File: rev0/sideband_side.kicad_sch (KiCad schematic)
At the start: 28 parts, among them IC1 ECP5-BGA256, U8 USB3343-CP

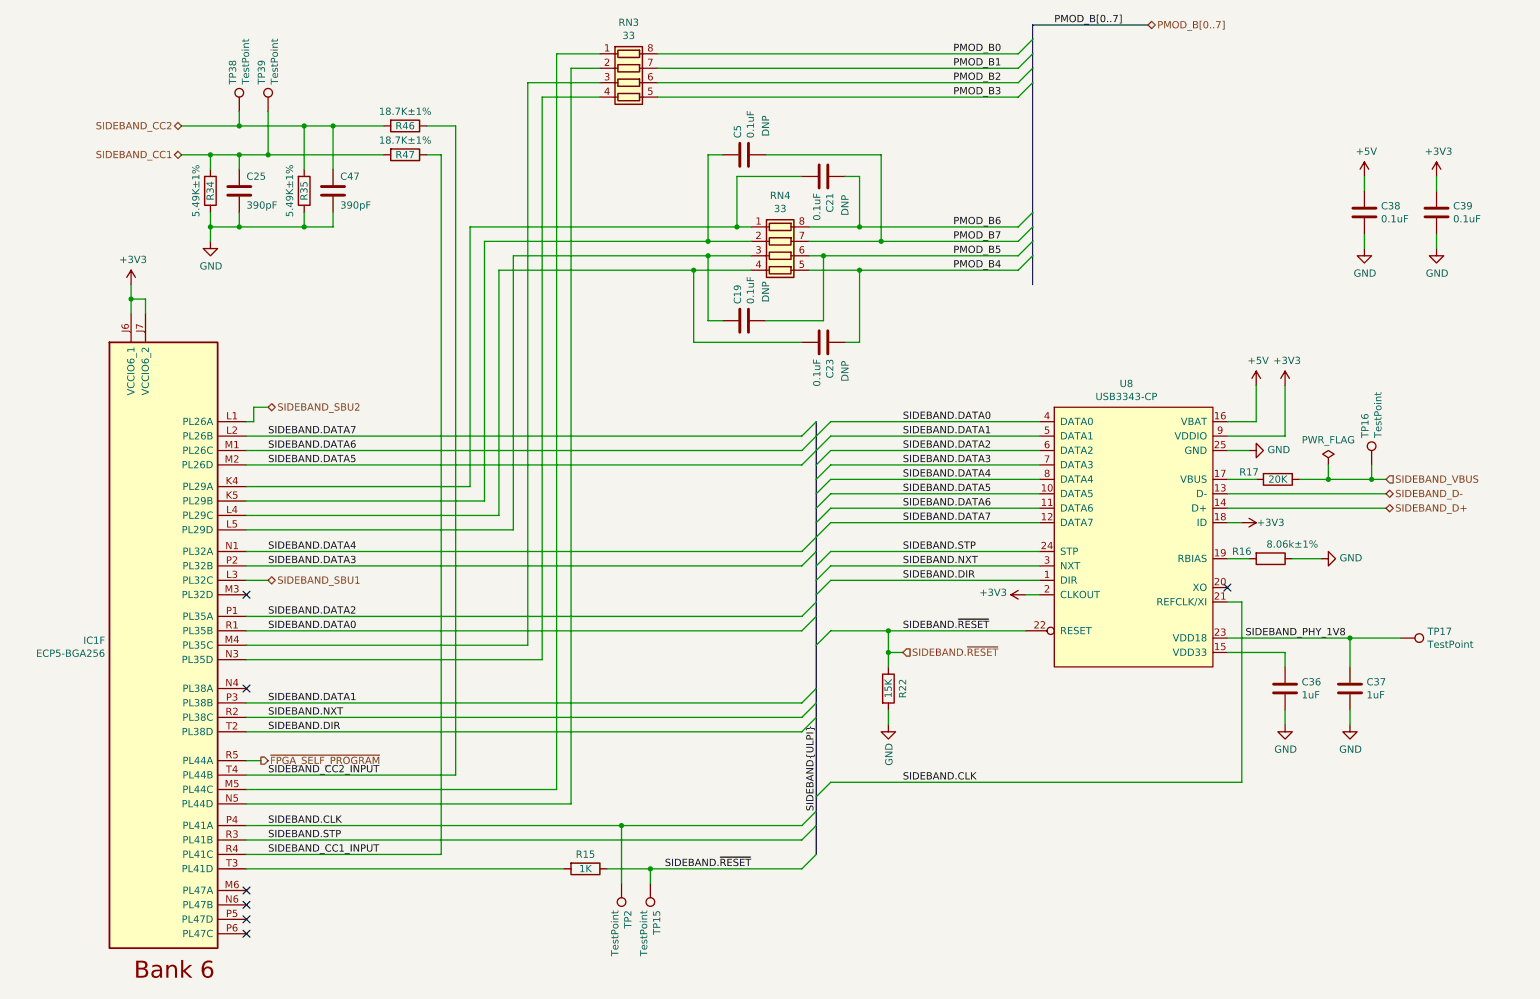
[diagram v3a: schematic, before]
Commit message: hardware: consistently use lowercase k for kilo
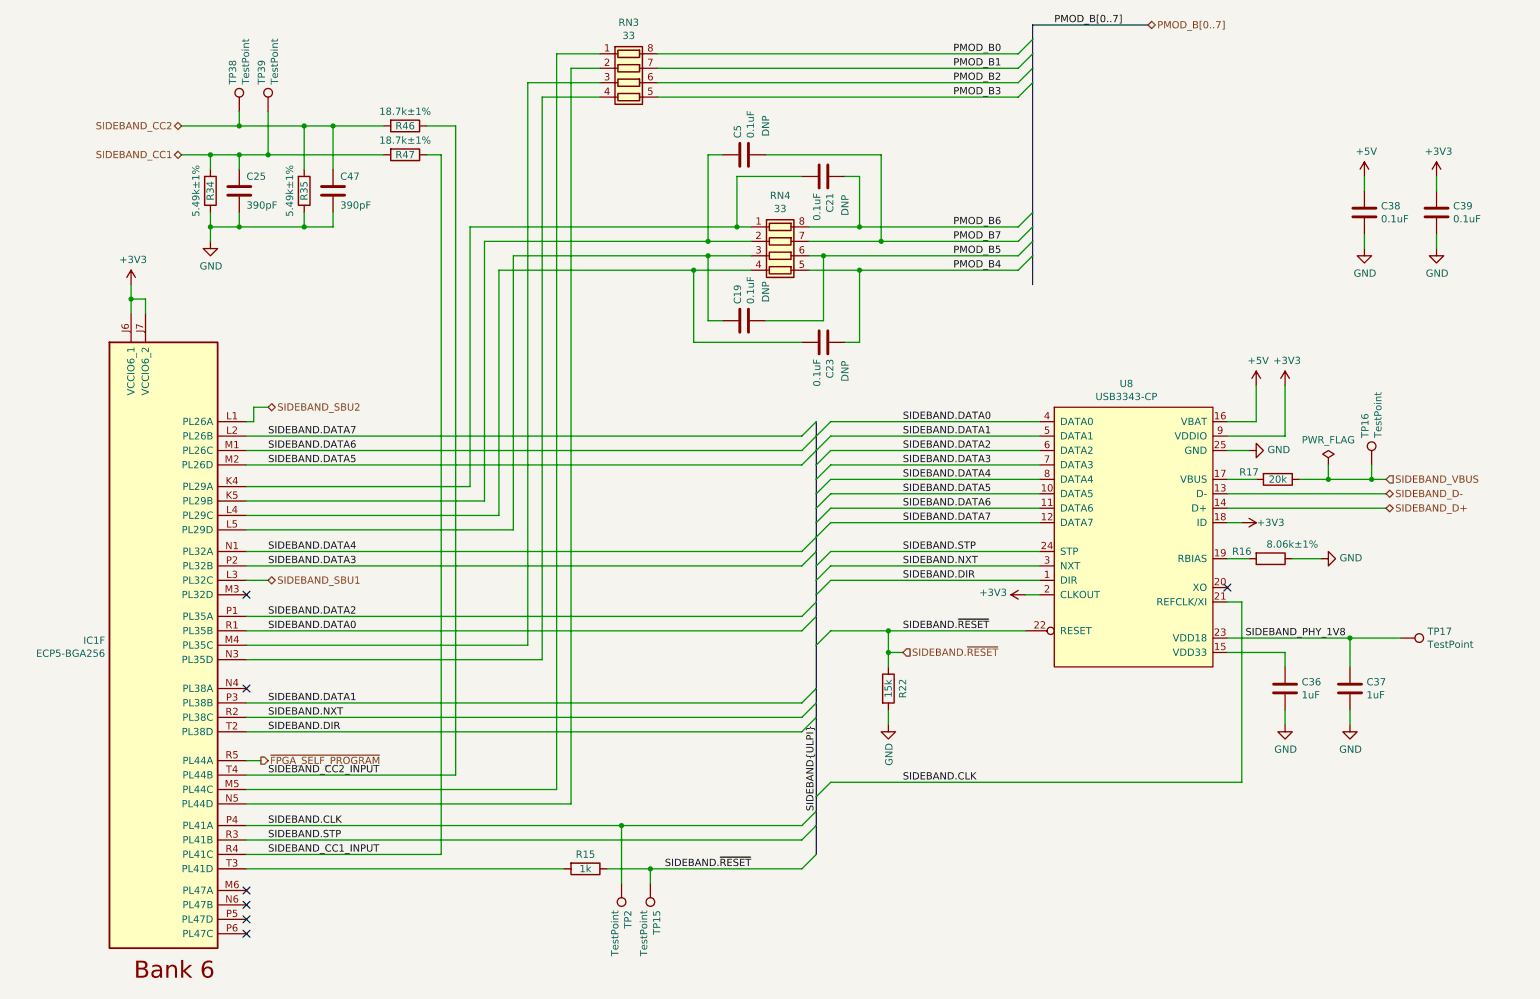
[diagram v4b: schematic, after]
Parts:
- R15: value 1K -> 1k
- R17: value 20K -> 20k
- R22: value 15K -> 15k
- R34, R35: value 5.49K±1% -> 5.49k±1%
- R46, R47: value 18.7K±1% -> 18.7k±1%
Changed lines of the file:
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@@
     (in_bom yes) (on_board yes)
     (property "Reference" "R17" (id 0) (at 229.87 95.25 90))
-    (property "Value" "20K" (id 1) (at 234.95 96.52 90))
+    (property "Value" "20k" (id 1) (at 234.95 96.52 90))
     (property "Footprint" "Resistor_SMD:R_0402_1005Metric" (id 2) (at 234.95 94.742 90)
       (effects (font (size 1.27 1.27)) hide)
@@
     (in_bom yes) (on_board yes)
     (property "Reference" "R15" (id 0) (at 113.03 162.56 90))
-    (property "Value" "1K" (id 1) (at 113.03 165.1 90))
+    (property "Value" "1k" (id 1) (at 113.03 165.1 90))
     (property "Footprint" "Resistor_SMD:R_0402_1005Metric" (id 2) (at 113.03 163.322 90)
       (effects (font (size 1.27 1.27)) hide)
@@
     (in_bom yes) (on_board yes)
     (property "Reference" "R22" (id 0) (at 168.91 133.35 90))
-    (property "Value" "15K" (id 1) (at 166.37 133.35 90))
+    (property "Value" "15k" (id 1) (at 166.37 133.35 90))
     (property "Footprint" "Resistor_SMD:R_0402_1005Metric" (id 2) (at 164.592 133.35 90)
       (effects (font (size 1.27 1.27)) hide)
@@
     (in_bom yes) (on_board yes)
     (property "Reference" "R46" (id 0) (at 81.28 34.29 90))
-    (property "Value" "18.7K±1%" (id 1) (at 81.28 31.75 90))
+    (property "Value" "18.7k±1%" (id 1) (at 81.28 31.75 90))
     (property "Footprint" "Resistor_SMD:R_0402_1005Metric" (id 2) (at 81.28 32.512 90)
       (effects (font (size 1.27 1.27)) hide)
@@
     (in_bom yes) (on_board yes)
     (property "Reference" "R47" (id 0) (at 81.28 39.37 90))
-    (property "Value" "18.7K±1%" (id 1) (at 81.28 36.83 90))
+    (property "Value" "18.7k±1%" (id 1) (at 81.28 36.83 90))
     (property "Footprint" "Resistor_SMD:R_0402_1005Metric" (id 2) (at 81.28 37.592 90)
       (effects (font (size 1.27 1.27)) hide)
@@
     (in_bom yes) (on_board yes)
     (property "Reference" "R34" (id 0) (at 46.99 45.72 90))
-    (property "Value" "5.49K±1%" (id 1) (at 44.45 45.72 90))
+    (property "Value" "5.49k±1%" (id 1) (at 44.45 45.72 90))
     (property "Footprint" "Resistor_SMD:R_0402_1005Metric" (id 2) (at 45.212 45.72 90)
       (effects (font (size 1.27 1.27)) hide)
@@
     (in_bom yes) (on_board yes)
     (property "Reference" "R35" (id 0) (at 63.5 45.72 90))
-    (property "Value" "5.49K±1%" (id 1) (at 60.96 45.72 90))
+    (property "Value" "5.49k±1%" (id 1) (at 60.96 45.72 90))
     (property "Footprint" "Resistor_SMD:R_0402_1005Metric" (id 2) (at 61.722 45.72 90)
       (effects (font (size 1.27 1.27)) hide)

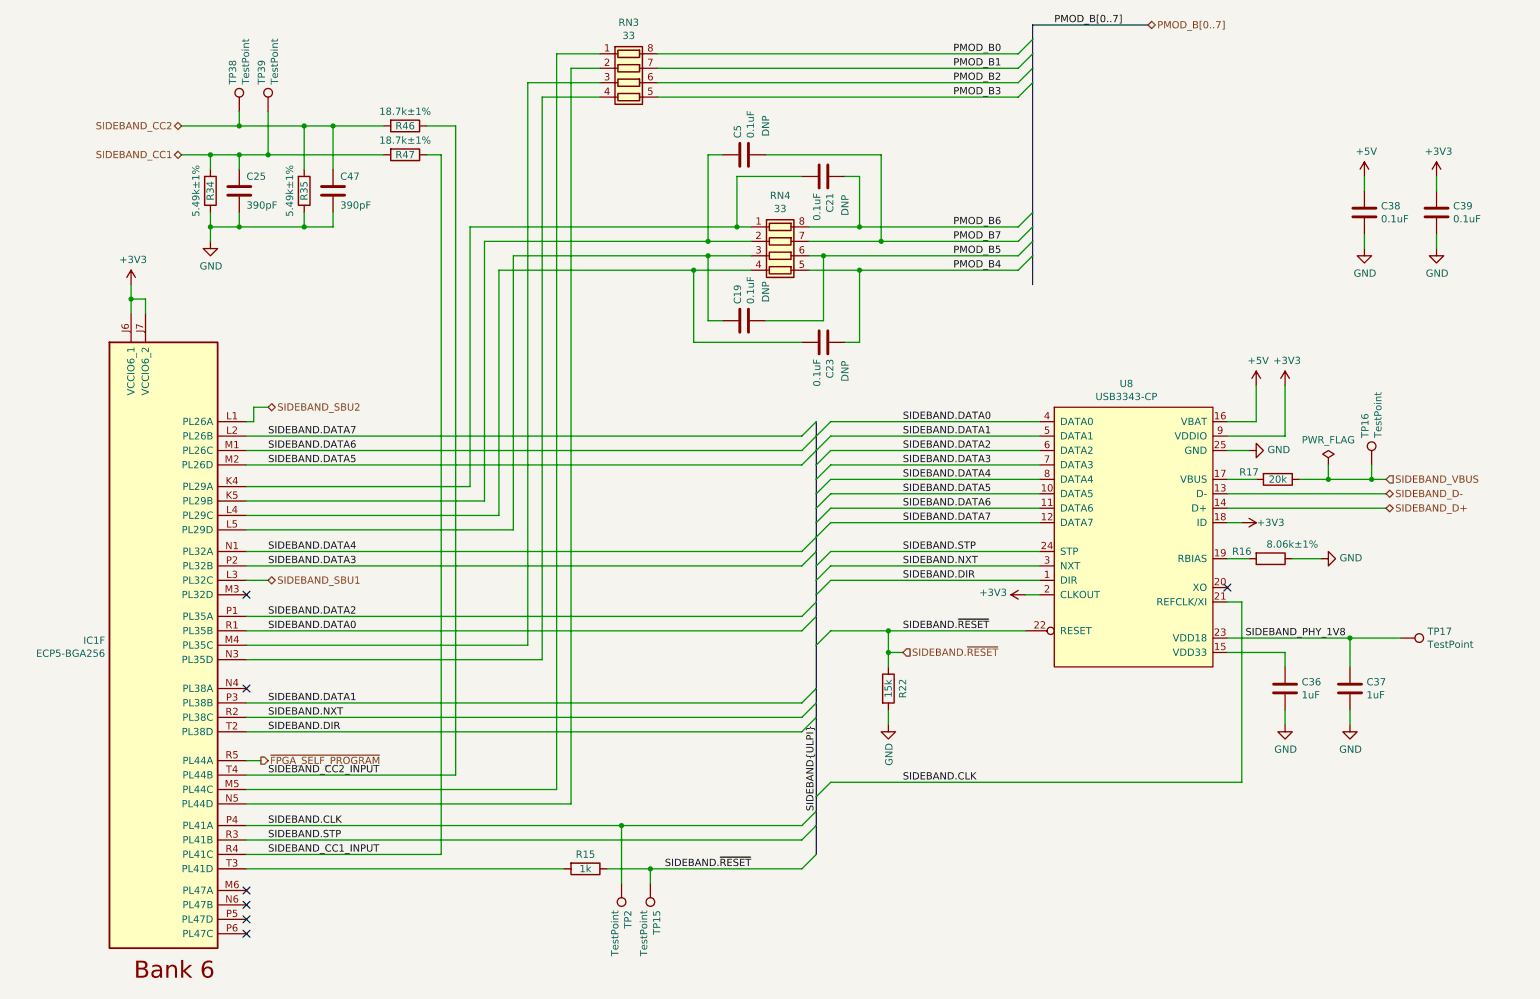
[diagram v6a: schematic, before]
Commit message: hardware: reassign FPGA I/O banks
assign HyperRAM to DQS group
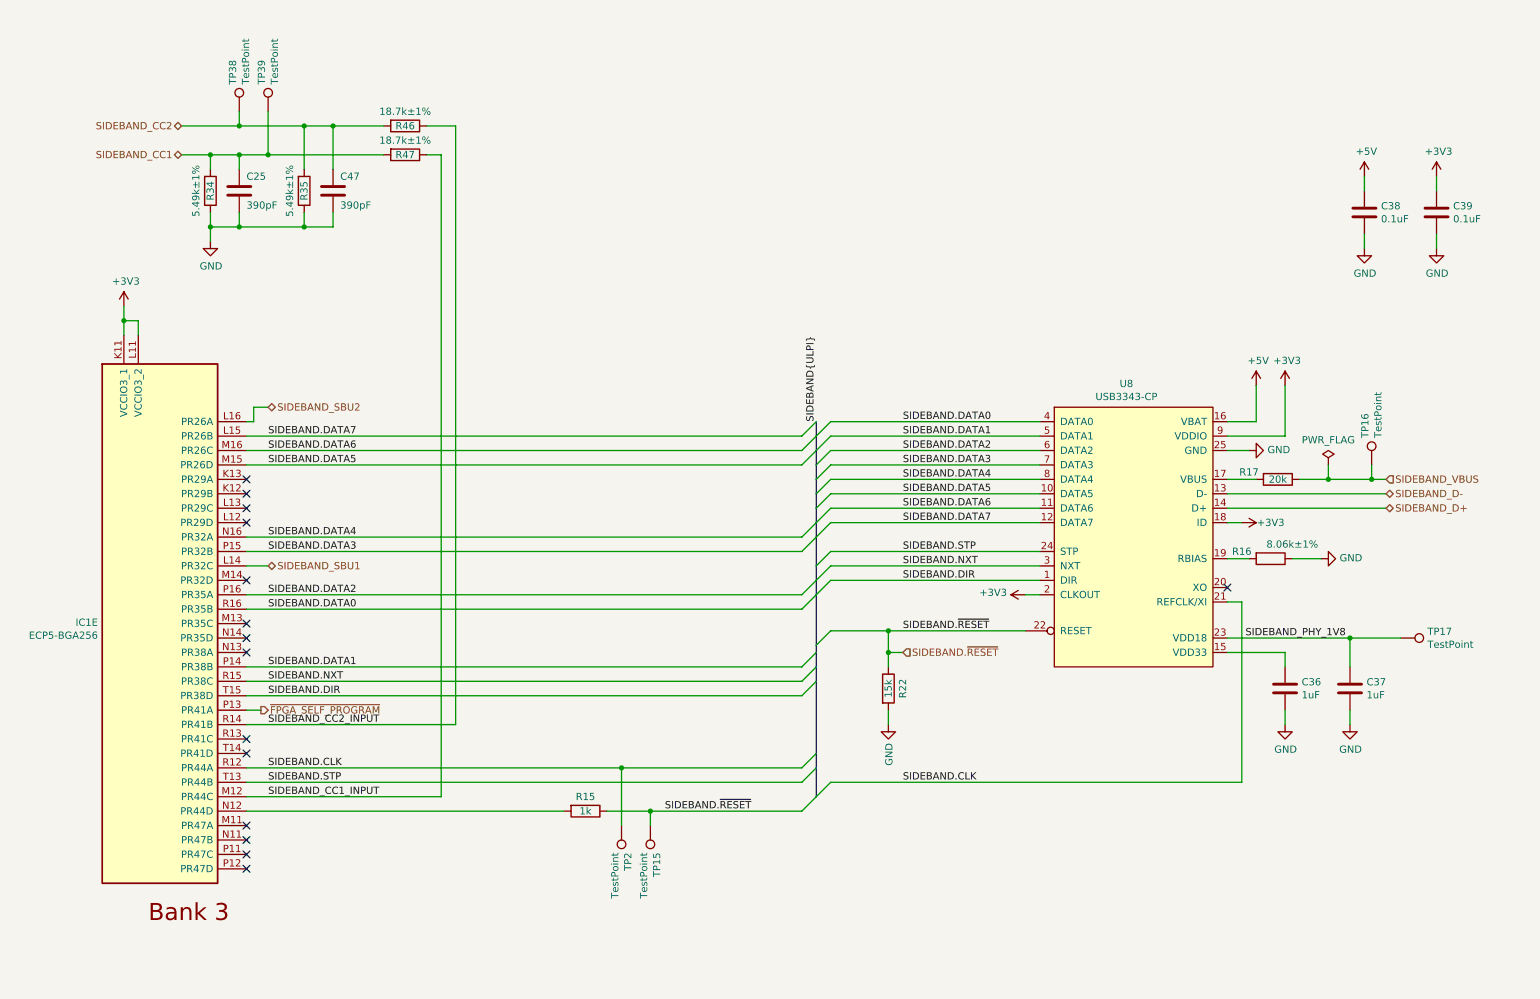
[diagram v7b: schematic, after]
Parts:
- removed C19, C21, C23, C5: 0.1uF, Capacitor_SMD:C_0402_1005Metric, symbol Device:C
- removed IC1: ECP5-BGA256, luna:lattice_cabga256, symbol fpgas_and_processors:ECP5-BGA256
- removed RN3, RN4: 33, Resistor_SMD:R_Array_Convex_4x0402, symbol Device:R_Pack04
- added IC1: ECP5-BGA256, luna:lattice_cabga256, symbol fpgas_and_processors:ECP5-BGA256
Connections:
- net +3V3: now also IC1.K11 (VCCIO3_1), IC1.L11 (VCCIO3_2)
- net SIDEBAND.CLK: now also IC1.R12 (PR44A)
- net SIDEBAND.DATA0: now also IC1.R16 (PR35B)
- net SIDEBAND.DATA1: now also IC1.P14 (PR38B)
- net SIDEBAND.DATA2: now also IC1.P16 (PR35A)
- net SIDEBAND.DATA3: now also IC1.P15 (PR32B)
- net SIDEBAND.DATA4: now also IC1.N16 (PR32A)
- net SIDEBAND.DATA5: now also IC1.M15 (PR26D)
- net SIDEBAND.DATA6: now also IC1.M16 (PR26C)
- net SIDEBAND.DATA7: now also IC1.L15 (PR26B)
- net SIDEBAND.DIR: now also IC1.T15 (PR38D)
- net SIDEBAND.NXT: now also IC1.R15 (PR38C)
- net SIDEBAND.STP: now also IC1.T13 (PR44B)
- net SIDEBAND_CC1_INPUT: now also IC1.M12 (PR44C)
- net SIDEBAND_CC2_INPUT: now also IC1.R14 (PR41B)
- net SIDEBAND_SBU1: now also IC1.L14 (PR32C)
- net SIDEBAND_SBU2: now also IC1.L16 (PR26A)
- net ~{FPGA_SELF_PROGRAM}: now also IC1.P13 (PR41A)
- net at R15.2: now also IC1.N12 (PR44D)
- no-connect marks 7 -> 15
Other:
- moved on the sheet: R15, TP15, TP2
